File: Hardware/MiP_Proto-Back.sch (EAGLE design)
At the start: 9 parts

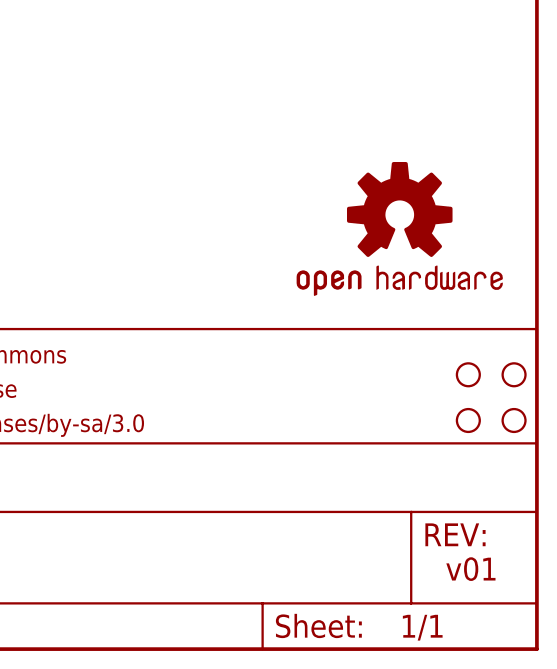
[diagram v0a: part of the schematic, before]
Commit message: changed rev numbers, added name to PCB.
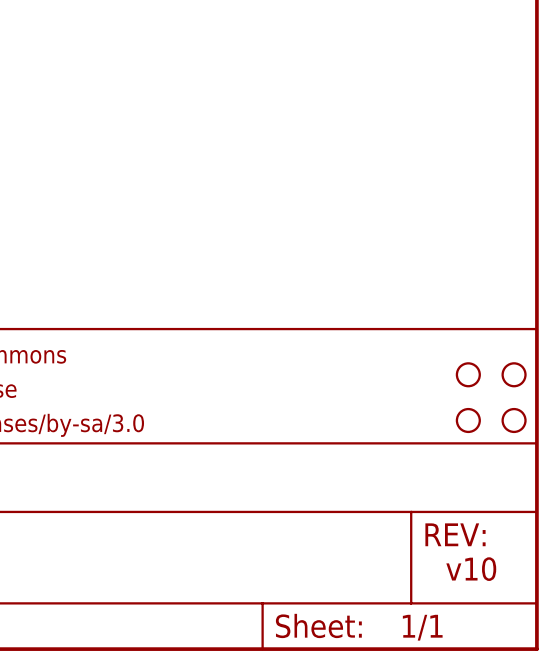
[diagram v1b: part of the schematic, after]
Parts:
- removed LOGO2: OSHW-LOGOS, SparkFun-Aesthetics:OSHW-LOGOS
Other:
- note added: "v10"
- note removed: "v01"
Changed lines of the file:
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@@
 <part name="STANDOFF3" library="SparkFun-Electromechanical" deviceset="STAND-OFF" device=""/>
 <part name="STANDOFF4" library="SparkFun-Electromechanical" deviceset="STAND-OFF" device=""/>
-<part name="LOGO2" library="SparkFun-Aesthetics" deviceset="OSHW-LOGO" device="S"/>
 <part name="JP1" library="SparkFun-Connectors" deviceset="M04" device="JST"/>
 <part name="JP2" library="SparkFun-Connectors" deviceset="M04" device="PTH"/>
@@
 <plain>
 <text x="167.64" y="10.16" size="2.54" layer="94">Casey Kuhns</text>
-<text x="238.76" y="7.62" size="2.54" layer="94">v01</text>
+<text x="238.76" y="7.62" size="2.54" layer="94">v10</text>
 </plain>
 <instances>
@@
 <instance part="STANDOFF3" gate="G$1" x="241.3" y="30.48"/>
 <instance part="STANDOFF4" gate="G$1" x="241.3" y="25.4"/>
-<instance part="LOGO2" gate="G$1" x="233.68" y="48.26"/>
 <instance part="JP1" gate="G$1" x="111.76" y="96.52"/>
 <instance part="JP2" gate="G$1" x="139.7" y="96.52" rot="MR0"/>
